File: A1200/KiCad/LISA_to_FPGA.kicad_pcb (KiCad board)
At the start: 4 copper layers, 64 x 37 mm, 39 parts, among them J1 Conn_01x01, J2 Conn_01x40, U1 LM1117-3.3, U2 74LVC162244ADGG, U3 74LVC162244ADGG, U4 LISA, U5 RP2354B

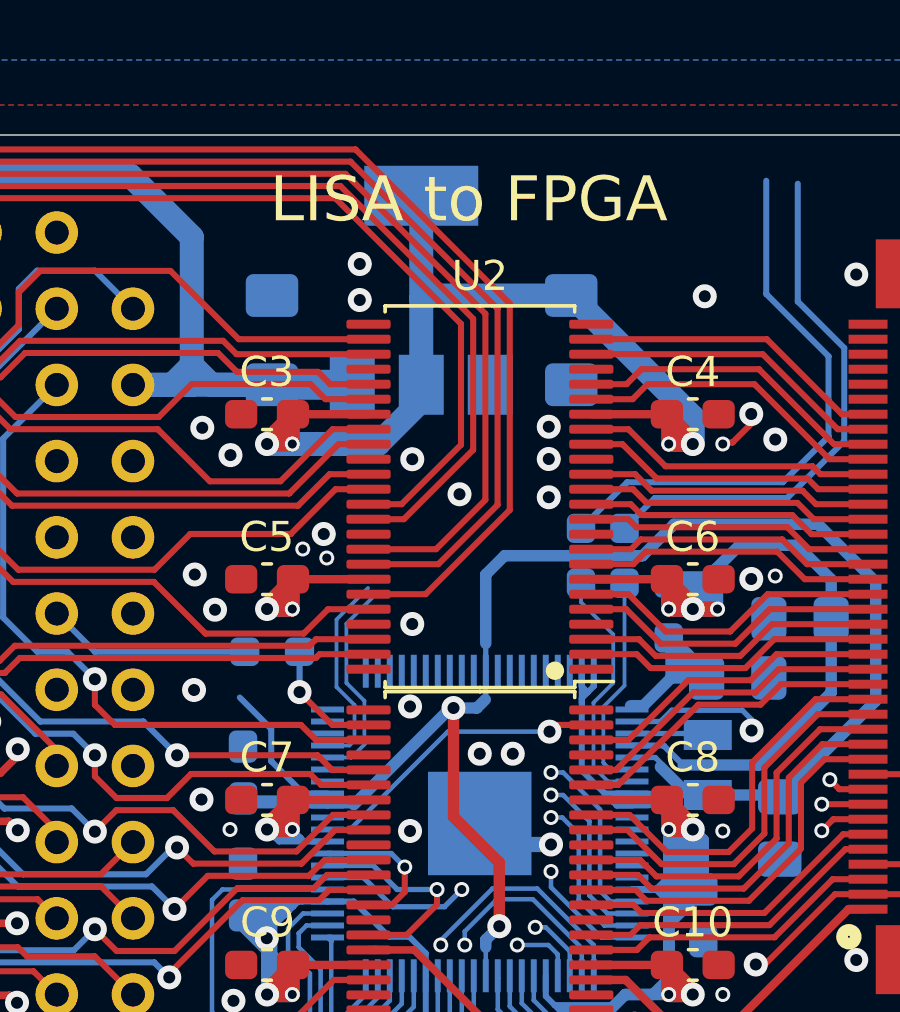
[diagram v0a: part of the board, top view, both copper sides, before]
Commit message: Add decoupling cap for pin 50 on QFN-80 footprint
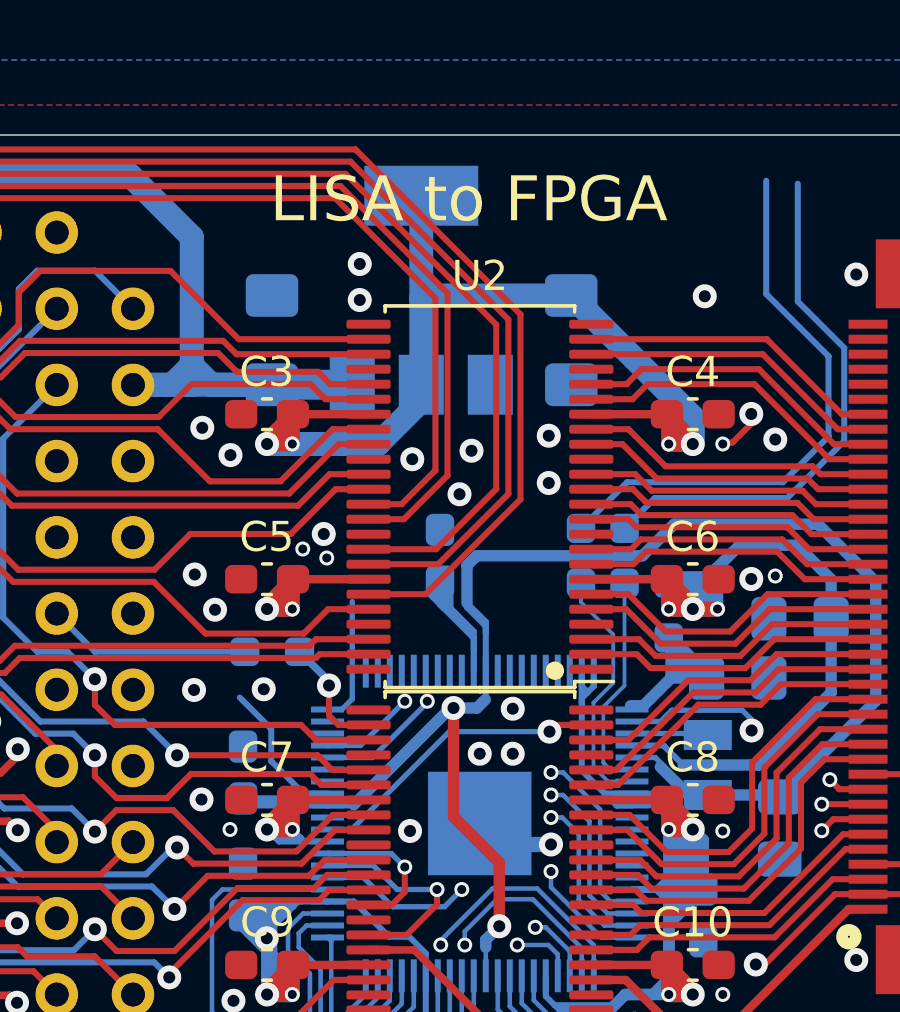
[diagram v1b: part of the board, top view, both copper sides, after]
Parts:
- added C19: 0.1uF, Capacitor_SMD:C_0603_1608Metric_Pad1.08x0.95mm_HandSolder, B.Cu at (192.2, 86.0)
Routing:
- net 3V3: track 226.6 -> 236.5 mm
- net Net-(U5-Pad40): track 0.00 -> 4.22 mm
- net RX: track 23.4 -> 20.9 mm, vias 1 -> 2
- net TX: track 23.4 -> 20.9 mm, vias 1 -> 2
- net 1V1: track 57.6 -> 60.1 mm
- net G1: track 37.5 -> 36.8 mm
- net G0: track 31.2 -> 30.5 mm

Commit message: Add decoupling cap for pin 59,60 on QFN-80 footprint, and change Csync pin hole to 0.8 mm
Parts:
- added C20: 0.1uF, Capacitor_SMD:C_0603_1608Metric_Pad1.08x0.95mm_HandSolder, B.Cu at (195.5, 86.0)
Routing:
- net 3V3: track 236.5 -> 248.8 mm, vias 19 -> 20
- net GND: track 22.2 -> 25.8 mm

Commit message: Add decoupling cap for pin 51 on QFN-80 footprint
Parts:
- added C21: 0.1uF, Capacitor_SMD:C_0603_1608Metric_Pad1.08x0.95mm_HandSolder, B.Cu at (194.0, 86.0)
- moved C19 0.35 mm to (192.6, 86.0)
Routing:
- net 1V1: track 60.3 -> 62.9 mm
- net 3V3: track 248.8 -> 247.1 mm

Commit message: Add external pull-up resistor on strapping pin GPIO33
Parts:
- added C22: 0.1uF, Capacitor_SMD:C_0603_1608Metric_Pad1.08x0.95mm_HandSolder, B.Cu at (189.7, 86.0)
- added R7: 4k7, Resistor_SMD:R_0603_1608Metric_Pad0.98x0.95mm_HandSolder, B.Cu at (191.1, 86.0)
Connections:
- U5 pad 40: Net-(U5-Pad40) -> GND
- U5 pad 42: Net-(U5-Pad42) -> /STRAP1
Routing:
- net 3V3: track 247.1 -> 273.6 mm
- net Net-(U5-Pad40): track 4.22 -> 0.00 mm
- net /STRAP1: track 0.00 -> 3.34 mm
- net GND: vias 44 -> 45

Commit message: Add decoupling cap for pin 10 on QFN-80 footprint
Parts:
- added C23: 0.1uF, Capacitor_SMD:C_0603_1608Metric_Pad1.08x0.95mm_HandSolder, B.Cu at (194.2, 103.3)
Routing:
- net 3V3: track 273.6 -> 313.6 mm
- net 1V1: track 62.9 -> 69.2 mm

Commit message: Add 100nF decoupling cap for pin 64 (VREG_VIN) on QFN-80 footprint
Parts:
- added C24: 0.1uF, Capacitor_SMD:C_0603_1608Metric_Pad1.08x0.95mm_HandSolder, B.Cu at (204.7, 91.9)
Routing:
- net GND: track 25.8 -> 27.2 mm
- net 1V1: track 69.2 -> 68.6 mm

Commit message: Add Micro-USB connector to the design
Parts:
- added J3: USB_B_Micro, LISA_to_FPGA:101181940001LF, F.Cu at (207.2, 105.9)
- moved J1 3.32 mm to (200.3, 107.1)
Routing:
- net USB_DP: track 18.9 -> 30.0 mm, vias 0 -> 1
- net USB_DM: track 17.7 -> 27.5 mm, vias 0 -> 1
- net CSYNC: track 17.3 -> 14.0 mm
- net 3V3: track 313.6 -> 316.7 mm
- net GND: vias 45 -> 43
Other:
- outline, holes or cut-outs redrawn

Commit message: Add a three-pin DEBUG-header with SWDIO,GND,SWCLK
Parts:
- removed the REF** at (206.5, 76.8)
- added J4: Conn_01x03, Connector_PinHeader_2.54mm:PinHeader_1x03_P2.54mm_Vertical, F.Cu at (208.2, 73.5)
- added REF**: OSHW-Symbol_6.7x6mm_SilkScreen, Symbol:OSHW-Symbol_6.7x6mm_SilkScreen, F.Cu at (166.8, 90.1)
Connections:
- U5 pad 33: /SWCLK -> SWCLK
- U5 pad 34: /SWDIO -> SWDIO
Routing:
- net SWDIO: track 0.00 -> 39.6 mm, vias 0 -> 1
- net SWCLK: track 0.00 -> 36.0 mm, vias 0 -> 1
- net /RUN: track 0.00 -> 25.1 mm, vias 0 -> 1
- net /SWCLK: track 4.88 -> 0.00 mm
- net 1V1: track 68.6 -> 65.3 mm
- net G7: track 41.2 -> 40.4 mm
- net GND: vias 43 -> 42
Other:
- board text added: "GND"
- board text added: "SWCLK"
- board text added: "SWDIO"
